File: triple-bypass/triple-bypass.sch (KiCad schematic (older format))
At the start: 1 part

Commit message: building the schematic
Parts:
- added C?: 220uF 10V, symbol CP
- added R?: 75.0, db-smt:0603, symbol R
- added R? (x4): 5.62k, db-smt:0603, symbol R
- added R? (x4): 1.00k, db-smt:0603, symbol R
- added R?: 100k, db-smt:0603, symbol R
- added U101: THS7374IPWR, symbol THS7374IPWR
- gave numbers to parts that had none: 1
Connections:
- net labels added: +5V, GND
- wire segments 0 -> 28
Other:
- moved on the sheet: CON101

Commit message: building the schematic
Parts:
- added B101, G101, R101, S101: TP50, db-smt:TP50, symbol TP50
- added J101: HDR1X2, db-thparts:HDR1X2, symbol HDR1X2
- added J102: HDR1X3, db-thparts:HDR1X3, symbol HDR1X3
- added R102: 2.20k, db-smt:0603, symbol R
- C101: renamed from C?; footprint (none) -> db-smt:SMD-6.6x6.6
- CON101: Description (none) -> CONN RCPT FMALE MINI DIN 9P SLDR; Digikey (none) -> CP-2290-ND
- U101: Description (none) -> IC SDTV VIDEO AMP 4-CH 14-TSSOP; Digikey (none) -> 296-41661-1-ND; Digikey# 296-41661-1-ND -> (none)
- gave numbers to parts that had none: 10
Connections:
- net labels added: SYNC-75, SYNC-OUT, SYNC-TTL
- wire segments 28 -> 45
- no-connect marks 0 -> 1

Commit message: building the schematic
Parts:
- added C? (x2): 0.1uF/50V, db-smt:0603, symbol C
- added C? (x3): 22uF/10V, db-smt:1206_P, symbol CP_1206
- added C? (x2): 270pF/50V, db-smt:0603, symbol C
- added R? (x2): 332, db-smt:0603, symbol R
- added R? (x2): 162k, db-smt:0603, symbol R
- added U? (x3): LMV358M8G-13, db-smt:TSSOP-8_3.0mm, symbol LMV358M8G-13
- C101: value 220uF 10V -> 220uF/10V
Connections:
- wire segments 45 -> 75
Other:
- note added: "0V to 1510mV signal swing, 2 V/V"
- note added: "0V to 5V signal swing on \nRGB from Genesis VDP"
- note added: "0V to 755mV signal swing \nafter voltage divider"
- note added: "CSYNC at video level always drives \nthe CVBS signal because I want \nmy HDRetrovision cables to work \nwith this thing!"
- note added: "CSYNC from Genesis VDP is \nopen collector output assuming \nthe mod has removed the \nGenesis' own 2.2k pull-up from \nthe signal path."
- note added: "Logic High on bypass disables \nthe internal filters, logic low \nenables them. Use pin jumper \nto force internal filter."
- note added: "Select video level or\nTTL csync"
- moved on the sheet: B101, C101, CON101, G101, J101, J102, R101, R102, R103, R104, R105, R106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

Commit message: first pass schematic done, not annotated yet
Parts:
- removed B101, G101, R101, S101: TP50, db-smt:TP50, symbol TP50
- added C? (x2): 10uF/10V, db-smt:0805, symbol C_0805
- added C? (x6): 1uF/16V, db-smt:0603, symbol C
- added C?: 0.1uF/50V, db-smt:0603, symbol C
- added R? (x2): 2.20k, db-smt:0603, symbol R
- added R? (x4): 75.0, db-smt:0603, symbol R
- added R?: 1.30k, db-smt:0603, symbol R
- added R? (x4): 130k, db-smt:0603, symbol R
- added R? (x2): 100k, db-smt:0603, symbol R
- added R? (x2): 6.19k, db-smt:0603, symbol R
- added R?: 511, db-smt:0603, symbol R
- added R?: 750, db-smt:0603, symbol R
- added TP? (x11): TP_50, db-smt:TP50, symbol TP_50
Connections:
- net labels added: SL, SR
- wire segments 75 -> 135
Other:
- note added: "0V to 5V signal \nswing on RGB \nfrom Genesis VDP"
- note added: "CSYNC at video level \nalways drives the CVBS \nsignal because bags of\nmoney from HD Retrovision"
- note removed: "0V to 5V signal swing on \nRGB from Genesis VDP"
- note removed: "CSYNC at video level always drives \nthe CVBS signal because I want \nmy HDRetrovision cables to work \nwith this thing!"
- moved on the sheet: C101, C?, CON101, J101, J102, R102, R103, R104, R105, R106, R107, R108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

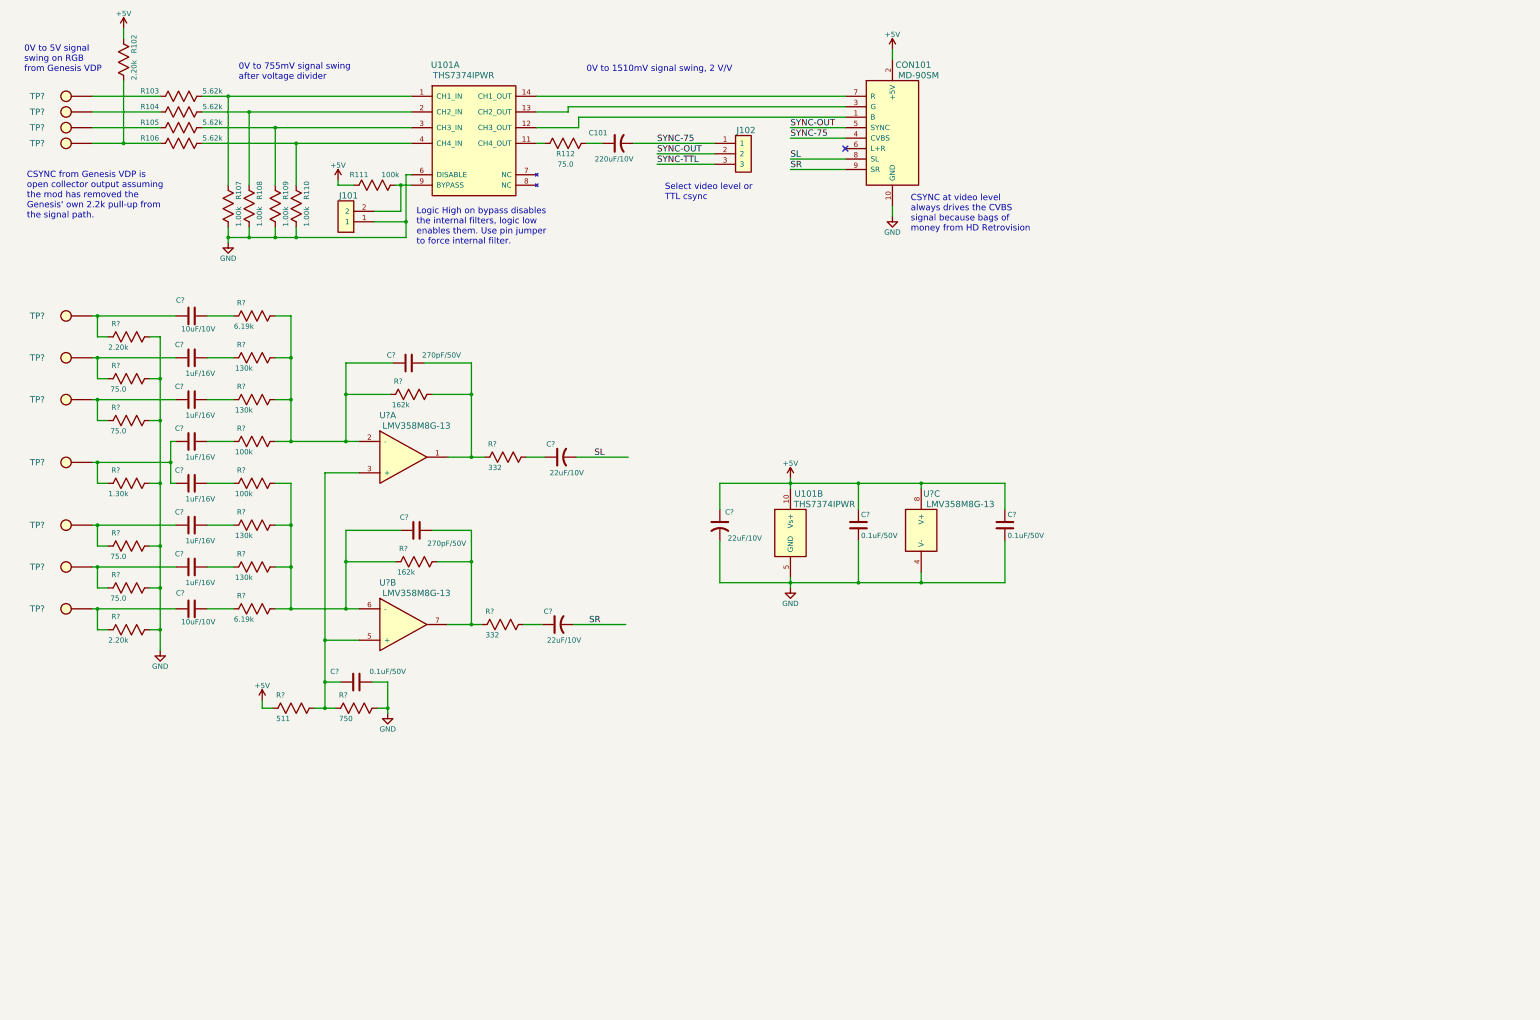
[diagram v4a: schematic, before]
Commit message: finalized and annotated schematic, waiting for review
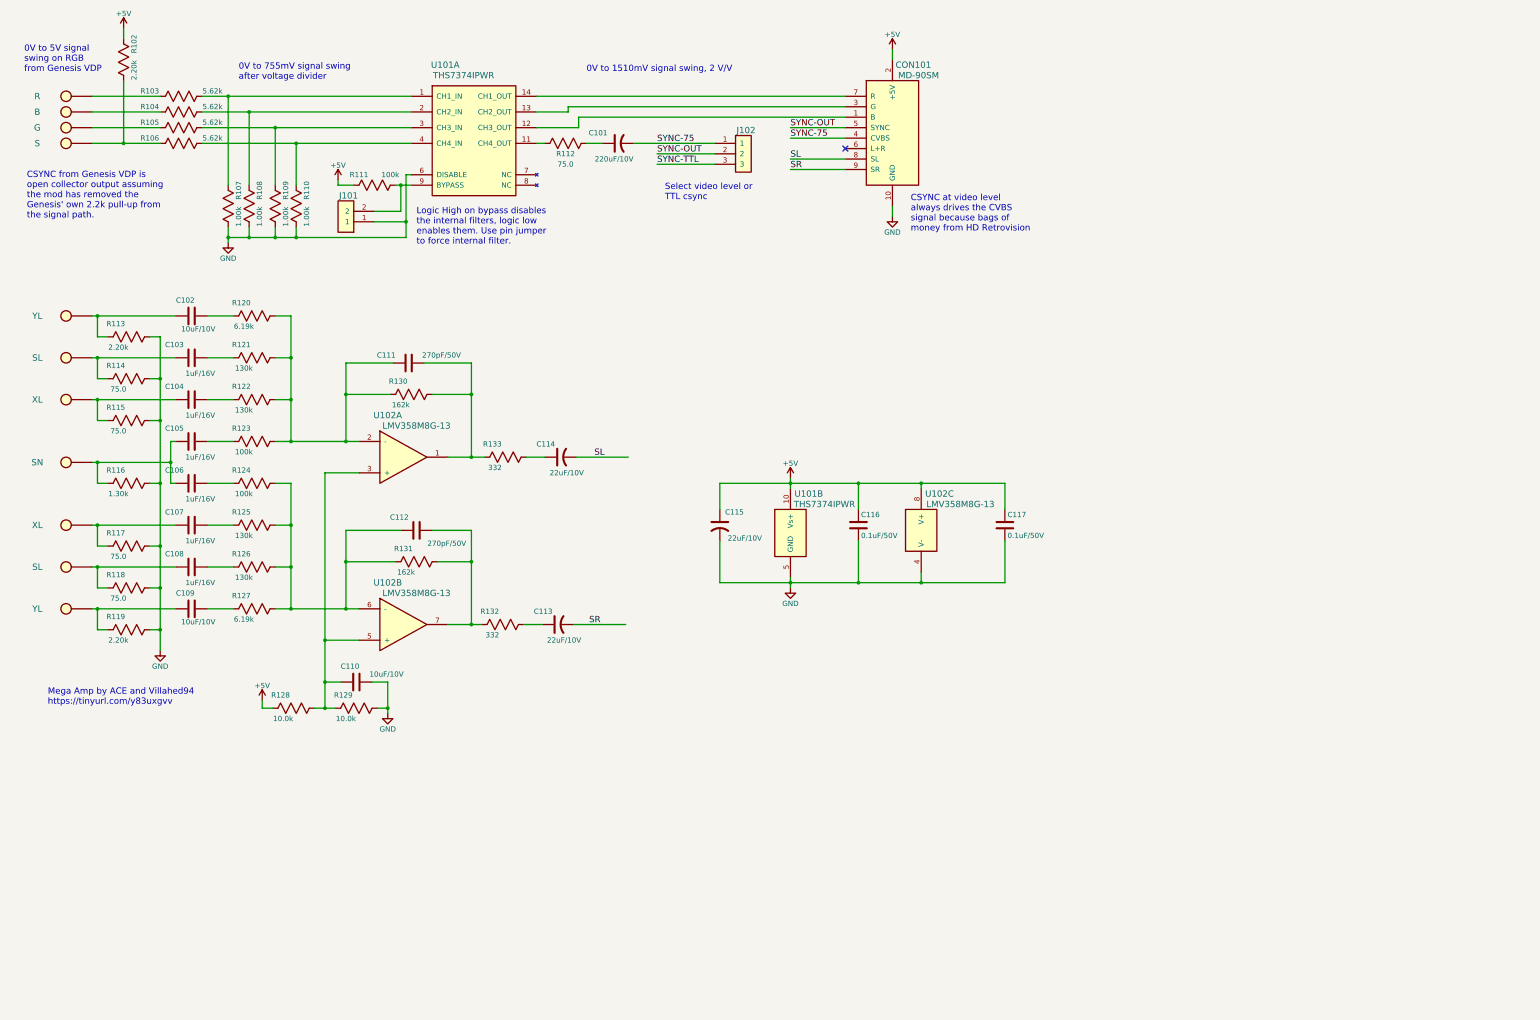
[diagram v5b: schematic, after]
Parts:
- removed C?: 0.1uF/50V, db-smt:0603, symbol C
- removed R?: 750, db-smt:0603, symbol R
- added C110: 10uF/10V, db-smt:0805, symbol C_0805
- added R129: 10.0k, db-smt:0603, symbol R
- R128: renamed from R?; value 511 -> 10.0k; Description RES 511 OHM 1/10W 1% 0603 SMD -> RES 10.0K OHM 1/10W 1% 0603 SMD; Digikey P511HCT-ND -> P10.0KHCT-ND
- gave numbers to parts that had none: 43
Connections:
- net GND: now also C110.1, R129.2
- net at R128.2, U102.3 (+), U102.5 (+): now also C110.2, R129.1
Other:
- note added: "Mega Amp by ACE and Villahed94\nhttps://tinyurl.com/y83uxgvv"

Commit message: added parts to PCB
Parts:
- U101: footprint (none) -> db-smt:TSSOP-14; Description (none) -> IC SDTV VIDEO AMP 4-CH 14-TSSOP; Digikey (none) -> 296-41661-1-ND
- renumbered B to B1, G to G1, R to R1, S to S1, SL to SL1, SL to SL2, SN to SN1, XL to XL1, XL to XL2, YL to YL1, YL to YL2
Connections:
- net SYNC-TTL: now also R102.1, R106.2, S1.1
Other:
- moved on the sheet: B1, G1, R1, S1
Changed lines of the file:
@@
 $EndDescr
 $Comp
-L THS7374IPWR U101
-U 2 1 5A68B50B
-P 7875 5450
-F 0 "U101" H 8200 5600 60  0000 C CNN
-F 1 "THS7374IPWR" H 8350 5500 60  0000 C CNN
-F 2 "" H 7875 5400 60  0001 C CNN
-F 3 "" H 7875 5400 60  0001 C CNN
-	2    7875 5450
-	1    0    0    -1
-$EndComp
-$Comp
-L +5V #PWR109
+L +5V #PWR01
 U 1 1 5A68CA11
 P 9000 1050
-F 0 "#PWR109" H 9000 900 50  0001 C CNN
+F 0 "#PWR01" H 9000 900 50  0001 C CNN
 F 1 "+5V" H 9000 1190 50  0000 C CNN
 F 2 "" H 9000 1050 50  0001 C CNN
@@
 $EndComp
 $Comp
-L GND #PWR110
+L GND #PWR02
 U 1 1 5A68CAEB
 P 9000 2650
-F 0 "#PWR110" H 9000 2400 50  0001 C CNN
+F 0 "#PWR02" H 9000 2400 50  0001 C CNN
 F 1 "GND" H 9000 2500 50  0000 C CNN
 F 2 "" H 9000 2650 50  0001 C CNN
@@
 $EndComp
 $Comp
-L GND #PWR103
+L GND #PWR03
 U 1 1 5A68EF32
 P 2650 2900
-F 0 "#PWR103" H 2650 2650 50  0001 C CNN
+F 0 "#PWR03" H 2650 2650 50  0001 C CNN
 F 1 "GND" H 2650 2750 50  0000 C CNN
 F 2 "" H 2650 2900 50  0001 C CNN
@@
 $EndComp
 $Comp
-L +5V #PWR105
+L +5V #PWR04
 U 1 1 5A68FF2A
 P 3700 2300
-F 0 "#PWR105" H 3700 2150 50  0001 C CNN
+F 0 "#PWR04" H 3700 2150 50  0001 C CNN
 F 1 "+5V" H 3700 2440 50  0000 C CNN
 F 2 "" H 3700 2300 50  0001 C CNN
@@
 $EndComp
 $Comp
-L +5V #PWR101
+L +5V #PWR05
 U 1 1 5A693A27
 P 1650 850
-F 0 "#PWR101" H 1650 700 50  0001 C CNN
+F 0 "#PWR05" H 1650 700 50  0001 C CNN
 F 1 "+5V" H 1650 990 50  0000 C CNN
 F 2 "" H 1650 850 50  0001 C CNN
 F 3 "" H 1650 850 50  0001 C CNN
 	1    1650 850
-	1    0    0    -1
-$EndComp
-$Comp
-L THS7374IPWR U101
-U 1 1 5A69691A
-P 4600 1400
-F 0 "U101" H 4725 1600 60  0000 C CNN
-F 1 "THS7374IPWR" H 4900 1500 60  0000 C CNN
-F 2 "db-smt:TSSOP-14" H 5025 1675 60  0001 C CNN
-F 3 "http://www.ti.com/lit/ds/symlink/ths7374.pdf" H 5675 1775 60  0001 C CNN
-F 4 "296-41661-1-ND" H 5025 1875 60  0001 C CNN "Digikey"
-F 5 "IC SDTV VIDEO AMP 4-CH 14-TSSOP" H 5450 1975 60  0001 C CNN "Description"
-	1    4600 1400
 	1    0    0    -1
 $EndComp
@@
 CSYNC at video level \nalways drives the CVBS \nsignal because bags of\nmoney from HD Retrovision
 $Comp
-L GND #PWR108
+L GND #PWR06
 U 1 1 5A6ACD1A
 P 8025 6200
-F 0 "#PWR108" H 8025 5950 50  0001 C CNN
+F 0 "#PWR06" H 8025 5950 50  0001 C CNN
 F 1 "GND" H 8025 6050 50  0000 C CNN
 F 2 "" H 8025 6200 50  0001 C CNN
@@
 $EndComp
 $Comp
-L +5V #PWR107
+L +5V #PWR07
 U 1 1 5A6ADA07
 P 8025 5150
-F 0 "#PWR107" H 8025 5000 50  0001 C CNN
+F 0 "#PWR07" H 8025 5000 50  0001 C CNN
 F 1 "+5V" H 8025 5290 50  0000 C CNN
 F 2 "" H 8025 5150 50  0001 C CNN
@@
 $EndComp
 $Comp
-L +5V #PWR104
+L +5V #PWR08
 U 1 1 5A6B0DB3
 P 2975 7275
-F 0 "#PWR104" H 2975 7125 50  0001 C CNN
+F 0 "#PWR08" H 2975 7125 50  0001 C CNN
 F 1 "+5V" H 2975 7415 50  0000 C CNN
 F 2 "" H 2975 7275 50  0001 C CNN
@@
 $EndComp
 $Comp
-L GND #PWR106
+L GND #PWR09
 U 1 1 5A6B0E82
 P 4175 7400
-F 0 "#PWR106" H 4175 7150 50  0001 C CNN
+F 0 "#PWR09" H 4175 7150 50  0001 C CNN
 F 1 "GND" H 4175 7250 50  0000 C CNN
 F 2 "" H 4175 7400 50  0001 C CNN
@@
 $EndComp
 $Comp
-L GND #PWR102
+L GND #PWR010
 U 1 1 5A6C4582
 P 2000 6800
-F 0 "#PWR102" H 2000 6550 50  0001 C CNN
+F 0 "#PWR010" H 2000 6550 50  0001 C CNN
 F 1 "GND" H 2000 6650 50  0000 C CNN
 F 2 "" H 2000 6800 50  0001 C CNN
@@
 	1650 850  1650 950
 Wire Wire Line
-	1350 1500 2000 1500
-Wire Wire Line
-	1350 1650 2000 1650
-Wire Wire Line
-	1350 1800 2000 1800
-Wire Wire Line
-	1350 1950 2000 1950
+	1150 1500 2000 1500
+Wire Wire Line
+	1150 1650 2000 1650
+Wire Wire Line
+	1150 1800 2000 1800
+Wire Wire Line
+	1150 1950 2000 1950
 Wire Wire Line
 	1650 1350 1650 1950
@@
 	4750 6550 5075 6550
 Wire Wire Line
-	3775 5650 3775 6400
+	3775 6400 3775 5650
 Wire Wire Line
 	3775 5650 4300 5650
@@
 	5675 4950 5500 4950
 Wire Wire Line
-	3775 4050 3775 4800
+	3775 4800 3775 4050
 Wire Wire Line
 	3775 4050 4225 4050
@@
 Connection ~ 2000 6600
 $Comp
-L TP_50 R
+L TP_50 R1
 U 1 1 5A6C9465
-P 1150 1500
-F 0 "R" H 825 1500 60  0000 C CNN
-F 1 "TP_50" H 1250 1700 60  0001 C CNN
-F 2 "db-smt:TP50" H 1450 1800 60  0001 C CNN
-F 3 "" H 1150 1450 60  0001 C CNN
-F 4 "#ND" H 1300 1800 60  0001 C CNN "Digikey"
-F 5 "0.05\" x 0.05\" SMT Test Point" H 1825 1900 60  0001 C CNN "Description"
-	1    1150 1500
-	1    0    0    -1
-$EndComp
-$Comp
-L TP_50 B
+P 950 1500
+F 0 "R1" H 625 1500 60  0000 C CNN
+F 1 "TP_50" H 1050 1700 60  0001 C CNN
+F 2 "db-smt:TP50" H 1250 1800 60  0001 C CNN
+F 3 "" H 950 1450 60  0001 C CNN
+F 4 "#ND" H 1100 1800 60  0001 C CNN "Digikey"
+F 5 "0.05\" x 0.05\" SMT Test Point" H 1625 1900 60  0001 C CNN "Description"
+	1    950  1500
+	1    0    0    -1
+$EndComp
+$Comp
+L TP_50 B1
 U 1 1 5A6C96BB
-P 1150 1650
-F 0 "B" H 825 1650 60  0000 C CNN
-F 1 "TP_50" H 1250 1850 60  0001 C CNN
-F 2 "db-smt:TP50" H 1450 1950 60  0001 C CNN
-F 3 "" H 1150 1600 60  0001 C CNN
-F 4 "#ND" H 1300 1950 60  0001 C CNN "Digikey"
-F 5 "0.05\" x 0.05\" SMT Test Point" H 1825 2050 60  0001 C CNN "Description"
-	1    1150 1650
-	1    0    0    -1
-$EndComp
-$Comp
-L TP_50 G
+P 950 1650
+F 0 "B1" H 625 1650 60  0000 C CNN
+F 1 "TP_50" H 1050 1850 60  0001 C CNN
+F 2 "db-smt:TP50" H 1250 1950 60  0001 C CNN
+F 3 "" H 950 1600 60  0001 C CNN
+F 4 "#ND" H 1100 1950 60  0001 C CNN "Digikey"
+F 5 "0.05\" x 0.05\" SMT Test Point" H 1625 2050 60  0001 C CNN "Description"
+	1    950  1650
+	1    0    0    -1
+$EndComp
+$Comp
+L TP_50 G1
 U 1 1 5A6C9788
-P 1150 1800
-F 0 "G" H 825 1800 60  0000 C CNN
-F 1 "TP_50" H 1250 2000 60  0001 C CNN
-F 2 "db-smt:TP50" H 1450 2100 60  0001 C CNN
-F 3 "" H 1150 1750 60  0001 C CNN
-F 4 "#ND" H 1300 2100 60  0001 C CNN "Digikey"
-F 5 "0.05\" x 0.05\" SMT Test Point" H 1825 2200 60  0001 C CNN "Description"
-	1    1150 1800
-	1    0    0    -1
-$EndComp
-$Comp
-L TP_50 S
+P 950 1800
+F 0 "G1" H 625 1800 60  0000 C CNN
+F 1 "TP_50" H 1050 2000 60  0001 C CNN
+F 2 "db-smt:TP50" H 1250 2100 60  0001 C CNN
+F 3 "" H 950 1750 60  0001 C CNN
+F 4 "#ND" H 1100 2100 60  0001 C CNN "Digikey"
+F 5 "0.05\" x 0.05\" SMT Test Point" H 1625 2200 60  0001 C CNN "Description"
+	1    950  1800
+	1    0    0    -1
+$EndComp
+$Comp
+L TP_50 S1
 U 1 1 5A6C9858
-P 1150 1950
-F 0 "S" H 825 1950 60  0000 C CNN
-F 1 "TP_50" H 1250 2150 60  0001 C CNN
-F 2 "db-smt:TP50" H 1450 2250 60  0001 C CNN
-F 3 "" H 1150 1900 60  0001 C CNN
-F 4 "#ND" H 1300 2250 60  0001 C CNN "Digikey"
-F 5 "0.05\" x 0.05\" SMT Test Point" H 1825 2350 60  0001 C CNN "Description"
-	1    1150 1950
-	1    0    0    -1
-$EndComp
-$Comp
-L TP_50 YL
+P 950 1950
+F 0 "S1" H 625 1950 60  0000 C CNN
+F 1 "TP_50" H 1050 2150 60  0001 C CNN
+F 2 "db-smt:TP50" H 1250 2250 60  0001 C CNN
+F 3 "" H 950 1900 60  0001 C CNN
+F 4 "#ND" H 1100 2250 60  0001 C CNN "Digikey"
+F 5 "0.05\" x 0.05\" SMT Test Point" H 1625 2350 60  0001 C CNN "Description"
+	1    950  1950
+	1    0    0    -1
+$EndComp
+$Comp
+L TP_50 YL1
 U 1 1 5A6C9968
 P 1150 3600
-F 0 "YL" H 825 3600 60  0000 C CNN
+F 0 "YL1" H 825 3600 60  0000 C CNN
 F 1 "TP_50" H 1250 3800 60  0001 C CNN
 F 2 "db-smt:TP50" H 1450 3900 60  0001 C CNN
@@
 Connection ~ 1400 3600
 $Comp
-L TP_50 SL
+L TP_50 SL1
 U 1 1 5A6CB5D9
 P 1150 4000
-F 0 "SL" H 825 4000 60  0000 C CNN
+F 0 "SL1" H 825 4000 60  0000 C CNN
 F 1 "TP_50" H 1250 4200 60  0001 C CNN
 F 2 "db-smt:TP50" H 1450 4300 60  0001 C CNN
@@
 $EndComp
 $Comp
-L TP_50 XL
+L TP_50 XL1
 U 1 1 5A6CB6C6
 P 1150 4400
-F 0 "XL" H 825 4400 60  0000 C CNN
+F 0 "XL1" H 825 4400 60  0000 C CNN
 F 1 "TP_50" H 1250 4600 60  0001 C CNN
 F 2 "db-smt:TP50" H 1450 4700 60  0001 C CNN
@@
 $EndComp
 $Comp
-L TP_50 SN
+L TP_50 SN1
 U 1 1 5A6CC1C8
 P 1150 5000
-F 0 "SN" H 825 5000 60  0000 C CNN
+F 0 "SN1" H 825 5000 60  0000 C CNN
 F 1 "TP_50" H 1250 5200 60  0001 C CNN
 F 2 "db-smt:TP50" H 1450 5300 60  0001 C CNN
@@
 Connection ~ 2000 5200
 $Comp
-L TP_50 XL
+L TP_50 XL2
 U 1 1 5A6CEA61
 P 1150 5600
-F 0 "XL" H 825 5600 60  0000 C CNN
+F 0 "XL2" H 825 5600 60  0000 C CNN
 F 1 "TP_50" H 1250 5800 60  0001 C CNN
 F 2 "db-smt:TP50" H 1450 5900 60  0001 C CNN
@@
 $EndComp
 $Comp
-L TP_50 SL
+L TP_50 SL2
 U 1 1 5A6CEB6B
 P 1150 6000
-F 0 "SL" H 825 6000 60  0000 C CNN
+F 0 "SL2" H 825 6000 60  0000 C CNN
 F 1 "TP_50" H 1250 6200 60  0001 C CNN
 F 2 "db-smt:TP50" H 1450 6300 60  0001 C CNN
@@
 $EndComp
 $Comp
-L TP_50 YL
+L TP_50 YL2
 U 1 1 5A6CEC64
 P 1150 6400
-F 0 "YL" H 825 6400 60  0000 C CNN
+F 0 "YL2" H 825 6400 60  0000 C CNN
 F 1 "TP_50" H 1250 6600 60  0001 C CNN
 F 2 "db-smt:TP50" H 1450 6700 60  0001 C CNN
@@
 Text Notes 925  7325 0    60   ~ 0
 Mega Amp by ACE and Villahed94\nhttps://tinyurl.com/y83uxgvv
+Text Label 1150 1950 0    60   ~ 0
+SYNC-TTL
+$Comp
+L THS7374IPWR U101
+U 1 1 5B619AF6
+P 4600 1400
+F 0 "U101" H 4725 1600 60  0000 C CNN
+F 1 "THS7374IPWR" H 4900 1500 60  0000 C CNN
+F 2 "db-smt:TSSOP-14" H 5025 1675 60  0001 C CNN
+F 3 "http://www.ti.com/lit/ds/symlink/ths7374.pdf" H 5675 1775 60  0001 C CNN
+F 4 "296-41661-1-ND" H 5025 1875 60  0001 C CNN "Digikey"
+F 5 "IC SDTV VIDEO AMP 4-CH 14-TSSOP" H 5450 1975 60  0001 C CNN "Description"
+	1    4600 1400
+	1    0    0    -1
+$EndComp
+$Comp
+L THS7374IPWR U101
+U 2 1 5B61A9A2
+P 7875 5450
+F 0 "U101" H 8225 5600 60  0000 C CNN
+F 1 "THS7374IPWR" H 8375 5500 60  0000 C CNN
+F 2 "db-smt:TSSOP-14" H 8300 5725 60  0001 C CNN
+F 3 "http://www.ti.com/lit/ds/symlink/ths7374.pdf" H 8950 5825 60  0001 C CNN
+F 4 "296-41661-1-ND" H 8300 5925 60  0001 C CNN "Digikey"
+F 5 "IC SDTV VIDEO AMP 4-CH 14-TSSOP" H 8725 6025 60  0001 C CNN "Description"
+	2    7875 5450
+	1    0    0    -1
+$EndComp
 $EndSCHEMATC
